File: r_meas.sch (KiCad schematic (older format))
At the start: 16 parts

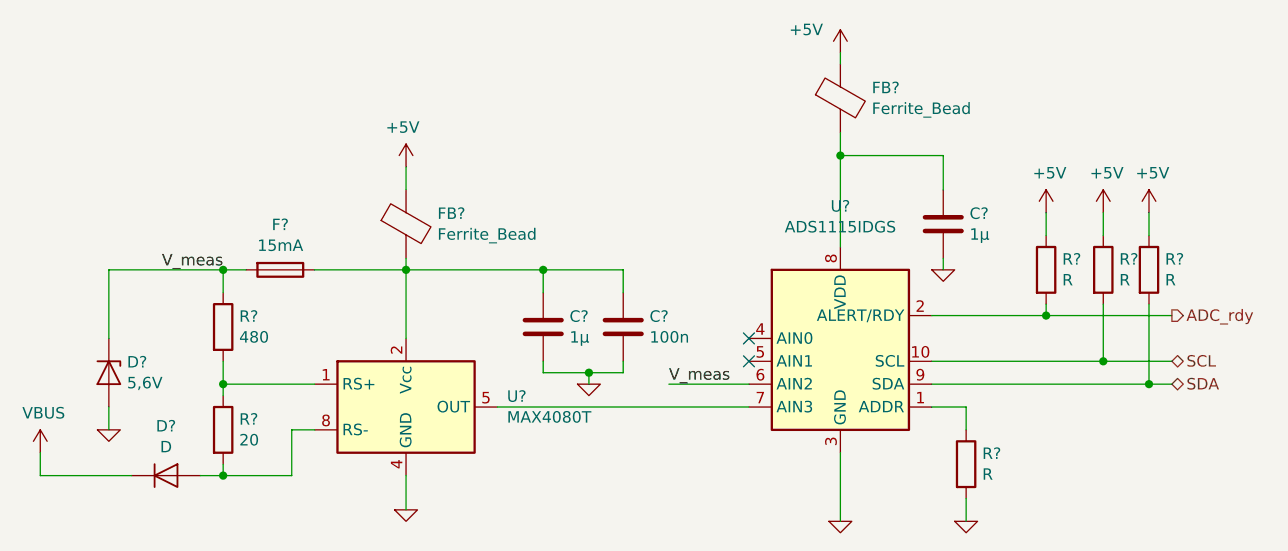
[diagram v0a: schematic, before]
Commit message: added pdf schematic
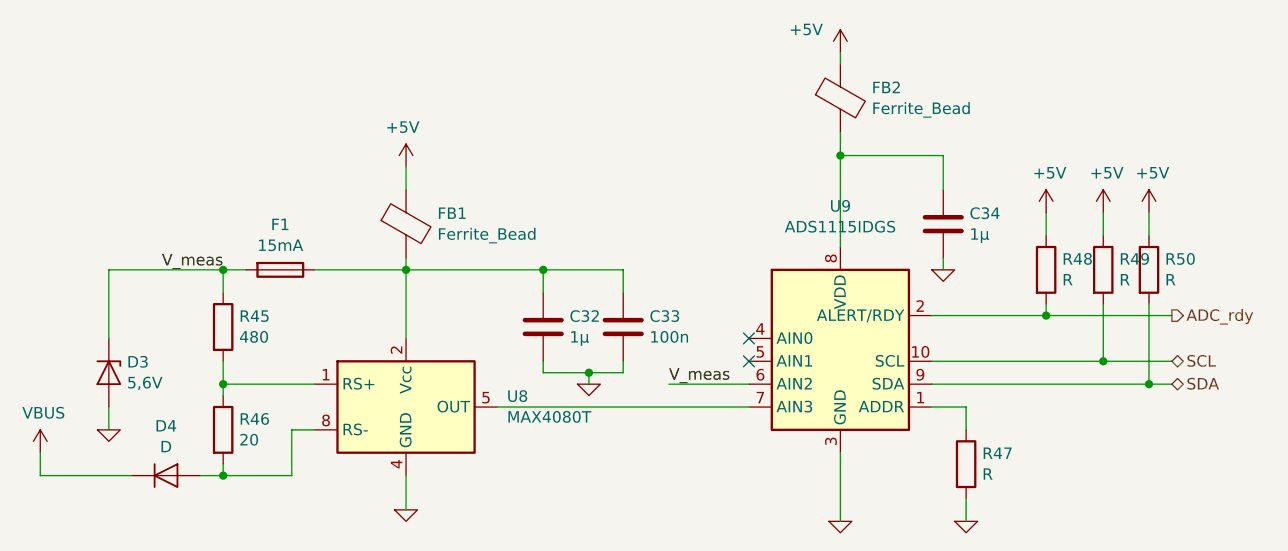
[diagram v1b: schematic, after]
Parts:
- gave numbers to parts that had none: 16
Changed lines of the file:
@@
 $EndDescr
 $Comp
-L Amplifier_Current:MAX4080T U?
+L Amplifier_Current:MAX4080T U8
 U 1 1 5D5C9028
 P 4150 3800
-F 0 "U?" H 4591 3846 50  0000 L CNN
+F 0 "U8" H 4591 3846 50  0000 L CNN
 F 1 "MAX4080T" H 4591 3755 50  0000 L CNN
 F 2 "" H 4800 3100 50  0001 C CNN
@@
 $EndComp
 $Comp
-L Analog_ADC:ADS1115IDGS U?
+L Analog_ADC:ADS1115IDGS U9
 U 1 1 5D5C90C4
 P 6050 3600
-F 0 "U?" H 6050 4278 50  0000 C CNN
+F 0 "U9" H 6050 4278 50  0000 C CNN
 F 1 "ADS1115IDGS" H 6050 4187 50  0000 C CNN
 F 2 "Package_SO:TSSOP-10_3x3mm_P0.5mm" H 6050 3100 50  0001 C CNN
@@
 $EndComp
 $Comp
-L Device:R R?
+L Device:R R49
 U 1 1 5D5C910D
 P 7200 3200
-F 0 "R?" H 7270 3246 50  0000 L CNN
+F 0 "R49" H 7270 3246 50  0000 L CNN
 F 1 "R" H 7270 3155 50  0000 L CNN
 F 2 "" V 7130 3200 50  0001 C CNN
@@
 $EndComp
 $Comp
-L Device:R R?
+L Device:R R50
 U 1 1 5D5C9157
 P 7400 3200
-F 0 "R?" H 7470 3246 50  0000 L CNN
+F 0 "R50" H 7470 3246 50  0000 L CNN
 F 1 "R" H 7470 3155 50  0000 L CNN
 F 2 "" V 7330 3200 50  0001 C CNN
@@
 SDA
 $Comp
-L power:+5V #PWR?
+L power:+5V #PWR067
 U 1 1 5D5C9230
 P 7200 2950
-F 0 "#PWR?" H 7200 2800 50  0001 C CNN
+F 0 "#PWR067" H 7200 2800 50  0001 C CNN
 F 1 "+5V" H 7215 3123 50  0000 C CNN
 F 2 "" H 7200 2950 50  0001 C CNN
@@
 $EndComp
 $Comp
-L power:+5V #PWR?
+L power:+5V #PWR062
 U 1 1 5D5C925D
 P 6050 2250
-F 0 "#PWR?" H 6050 2100 50  0001 C CNN
+F 0 "#PWR062" H 6050 2100 50  0001 C CNN
 F 1 "+5V" H 5900 2350 50  0000 C CNN
 F 2 "" H 6050 2250 50  0001 C CNN
@@
 $EndComp
 $Comp
-L power:+5V #PWR?
+L power:+5V #PWR059
 U 1 1 5D5C9278
 P 4150 2750
-F 0 "#PWR?" H 4150 2600 50  0001 C CNN
+F 0 "#PWR059" H 4150 2600 50  0001 C CNN
 F 1 "+5V" H 4165 2923 50  0000 C CNN
 F 2 "" H 4150 2750 50  0001 C CNN
@@
 $EndComp
 $Comp
-L power:+5V #PWR?
+L power:+5V #PWR068
 U 1 1 5D5C928B
 P 7400 2950
-F 0 "#PWR?" H 7400 2800 50  0001 C CNN
+F 0 "#PWR068" H 7400 2800 50  0001 C CNN
 F 1 "+5V" H 7415 3123 50  0000 C CNN
 F 2 "" H 7400 2950 50  0001 C CNN
@@
 $EndComp
 $Comp
-L Device:C C?
+L Device:C C34
 U 1 1 5D5C92DB
 P 6500 3000
-F 0 "C?" H 6615 3046 50  0000 L CNN
+F 0 "C34" H 6615 3046 50  0000 L CNN
 F 1 "1µ" H 6615 2955 50  0000 L CNN
 F 2 "" H 6538 2850 50  0001 C CNN
@@
 $EndComp
 $Comp
-L Device:Ferrite_Bead FB?
+L Device:Ferrite_Bead FB1
 U 1 1 5D5C936F
 P 4150 3000
-F 0 "FB?" H 4287 3046 50  0000 L CNN
+F 0 "FB1" H 4287 3046 50  0000 L CNN
 F 1 "Ferrite_Bead" H 4287 2955 50  0000 L CNN
 F 2 "" V 4080 3000 50  0001 C CNN
@@
 	6050 2700 6050 3100
 $Comp
-L daisy:GND #PWR?
+L daisy:GND #PWR064
 U 1 1 5D5C9638
 P 6500 3200
-F 0 "#PWR?" H 6500 3200 30  0001 C CNN
+F 0 "#PWR064" H 6500 3200 30  0001 C CNN
 F 1 "GND" H 6500 3130 30  0001 C CNN
 F 2 "" H 6500 3200 60  0000 C CNN
@@
 	7400 2950 7400 3050
 $Comp
-L Device:R R?
+L Device:R R47
 U 1 1 5D5C9A6F
 P 6600 4050
-F 0 "R?" H 6670 4096 50  0000 L CNN
+F 0 "R47" H 6670 4096 50  0000 L CNN
 F 1 "R" H 6670 4005 50  0000 L CNN
 F 2 "" V 6530 4050 50  0001 C CNN
@@
 $EndComp
 $Comp
-L daisy:GND #PWR?
+L daisy:GND #PWR065
 U 1 1 5D5C9AED
 P 6600 4300
-F 0 "#PWR?" H 6600 4300 30  0001 C CNN
+F 0 "#PWR065" H 6600 4300 30  0001 C CNN
 F 1 "GND" H 6600 4230 30  0001 C CNN
 F 2 "" H 6600 4300 60  0000 C CNN
@@
 $EndComp
 $Comp
-L daisy:GND #PWR?
+L daisy:GND #PWR063
 U 1 1 5D5C9B06
 P 6050 4300
-F 0 "#PWR?" H 6050 4300 30  0001 C CNN
+F 0 "#PWR063" H 6050 4300 30  0001 C CNN
 F 1 "GND" H 6050 4230 30  0001 C CNN
 F 2 "" H 6050 4300 60  0000 C CNN
@@
 	5650 3800 4550 3800
 $Comp
-L daisy:GND #PWR?
+L daisy:GND #PWR060
 U 1 1 5D5CA317
 P 4150 4250
-F 0 "#PWR?" H 4150 4250 30  0001 C CNN
+F 0 "#PWR060" H 4150 4250 30  0001 C CNN
 F 1 "GND" H 4150 4180 30  0001 C CNN
 F 2 "" H 4150 4250 60  0000 C CNN
@@
 	4150 4250 4150 4100
 $Comp
-L Device:C C?
+L Device:C C32
 U 1 1 5D5CA738
 P 4750 3450
-F 0 "C?" H 4865 3496 50  0000 L CNN
+F 0 "C32" H 4865 3496 50  0000 L CNN
 F 1 "1µ" H 4865 3405 50  0000 L CNN
 F 2 "" H 4788 3300 50  0001 C CNN
@@
 	4150 2850 4150 2750
 $Comp
-L Device:C C?
+L Device:C C33
 U 1 1 5D5CAD2B
 P 5100 3450
-F 0 "C?" H 5215 3496 50  0000 L CNN
+F 0 "C33" H 5215 3496 50  0000 L CNN
 F 1 "100n" H 5215 3405 50  0000 L CNN
 F 2 "" H 5138 3300 50  0001 C CNN
@@
 	4950 3650 5100 3650
 $Comp
-L daisy:GND #PWR?
+L daisy:GND #PWR061
 U 1 1 5D5CBDC2
 P 4950 3700
-F 0 "#PWR?" H 4950 3700 30  0001 C CNN
+F 0 "#PWR061" H 4950 3700 30  0001 C CNN
 F 1 "GND" H 4950 3630 30  0001 C CNN
 F 2 "" H 4950 3700 60  0000 C CNN
@@
 $EndComp
 $Comp
-L Device:Fuse F?
+L Device:Fuse F1
 U 1 1 5D5CC9A1
 P 3600 3200
-F 0 "F?" V 3403 3200 50  0000 C CNN
+F 0 "F1" V 3403 3200 50  0000 C CNN
 F 1 "15mA" V 3494 3200 50  0000 C CNN
 F 2 "" V 3530 3200 50  0001 C CNN
@@
 	3750 3200 4150 3200
 $Comp
-L Device:D_Zener D?
+L Device:D_Zener D3
 U 1 1 5D5CD013
 P 2850 3650
-F 0 "D?" V 2804 3729 50  0000 L CNN
+F 0 "D3" V 2804 3729 50  0000 L CNN
 F 1 "5,6V" V 2895 3729 50  0000 L CNN
 F 2 "" H 2850 3650 50  0001 C CNN
@@
 $EndComp
 $Comp
-L Device:R R?
+L Device:R R45
 U 1 1 5D5CD0A1
 P 3350 3450
-F 0 "R?" H 3420 3496 50  0000 L CNN
+F 0 "R45" H 3420 3496 50  0000 L CNN
 F 1 "480" H 3420 3405 50  0000 L CNN
 F 2 "" V 3280 3450 50  0001 C CNN
@@
 $EndComp
 $Comp
-L Device:R R?
+L Device:R R46
 U 1 1 5D5CD0E5
 P 3350 3900
-F 0 "R?" H 3420 3946 50  0000 L CNN
+F 0 "R46" H 3420 3946 50  0000 L CNN
 F 1 "20" H 3420 3855 50  0000 L CNN
 F 2 "" V 3280 3900 50  0001 C CNN
@@
 $EndComp
 $Comp
-L daisy:GND #PWR?
+L daisy:GND #PWR058
 U 1 1 5D5CD174
 P 2850 3900
-F 0 "#PWR?" H 2850 3900 30  0001 C CNN
+F 0 "#PWR058" H 2850 3900 30  0001 C CNN
 F 1 "GND" H 2850 3830 30  0001 C CNN
 F 2 "" H 2850 3900 60  0000 C CNN
@@
 	5300 3700 5650 3700
 $Comp
-L Device:Ferrite_Bead FB?
+L Device:Ferrite_Bead FB2
 U 1 1 5D5D2DEC
 P 6050 2450
-F 0 "FB?" H 6187 2496 50  0000 L CNN
+F 0 "FB2" H 6187 2496 50  0000 L CNN
 F 1 "Ferrite_Bead" H 6187 2405 50  0000 L CNN
 F 2 "" V 5980 2450 50  0001 C CNN
@@
 $EndComp
 $Comp
-L Device:D D?
+L Device:D D4
 U 1 1 5D5D348E
 P 3100 4100
-F 0 "D?" H 3100 4316 50  0000 C CNN
+F 0 "D4" H 3100 4316 50  0000 C CNN
 F 1 "D" H 3100 4225 50  0000 C CNN
 F 2 "" H 3100 4100 50  0001 C CNN
@@
 Connection ~ 3350 4100
 $Comp
-L power:VBUS #PWR?
+L power:VBUS #PWR057
 U 1 1 5D5D4099
 P 2550 4000
-F 0 "#PWR?" H 2550 3850 50  0001 C CNN
+F 0 "#PWR057" H 2550 3850 50  0001 C CNN
 F 1 "VBUS" H 2565 4173 50  0000 C CNN
 F 2 "" H 2550 4000 50  0001 C CNN
@@
 	2550 4100 2550 4000
 $Comp
-L Device:R R?
+L Device:R R48
 U 1 1 5D5D66BA
 P 6950 3200
-F 0 "R?" H 7020 3246 50  0000 L CNN
+F 0 "R48" H 7020 3246 50  0000 L CNN
 F 1 "R" H 7020 3155 50  0000 L CNN
 F 2 "" V 6880 3200 50  0001 C CNN
@@
 	6950 3400 6950 3350
 $Comp
-L power:+5V #PWR?
+L power:+5V #PWR066
 U 1 1 5D5DCDE2
 P 6950 2950
-F 0 "#PWR?" H 6950 2800 50  0001 C CNN
+F 0 "#PWR066" H 6950 2800 50  0001 C CNN
 F 1 "+5V" H 6965 3123 50  0000 C CNN
 F 2 "" H 6950 2950 50  0001 C CNN

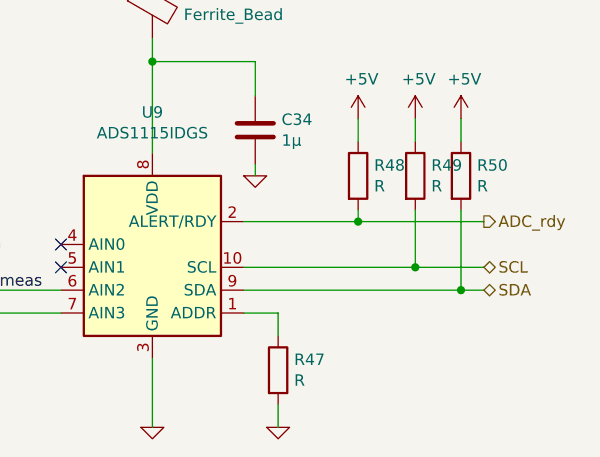
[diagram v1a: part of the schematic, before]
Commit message: started assigning footprints
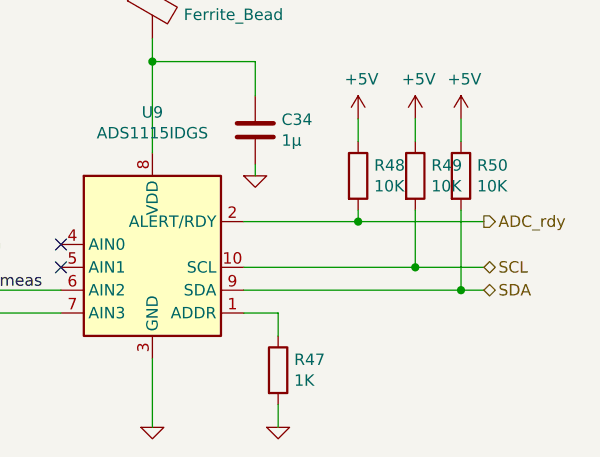
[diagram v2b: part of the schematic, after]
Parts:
- C32, C34: footprint (none) -> Capacitor_SMD:C_1206_3216Metric
- C33: footprint (none) -> Capacitor_SMD:C_0603_1608Metric
- D3, D4: footprint (none) -> Diode_SMD:D_1206_3216Metric
- F1: footprint (none) -> Fuse:Fuse_1206_3216Metric
- FB1, FB2: footprint (none) -> Inductor_SMD:L_1206_3216Metric
- R45, R46: footprint (none) -> Resistor_SMD:R_0603_1608Metric
- R47: value R -> 1K; footprint (none) -> Resistor_SMD:R_0603_1608Metric
- R48, R49, R50: value R -> 10K; footprint (none) -> Resistor_SMD:R_0603_1608Metric
- U8: footprint (none) -> Package_SO:SOIC-8_3.9x4.9mm_P1.27mm
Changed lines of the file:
@@
 F 0 "U8" H 4591 3846 50  0000 L CNN
 F 1 "MAX4080T" H 4591 3755 50  0000 L CNN
-F 2 "" H 4800 3100 50  0001 C CNN
+F 2 "Package_SO:SOIC-8_3.9x4.9mm_P1.27mm" H 4800 3100 50  0001 C CNN
 F 3 "http://datasheets.maximintegrated.com/en/ds/MAX4080-MAX4081.pdf" H 4150 4200 50  0001 C CNN
 	1    4150 3800
@@
 P 7200 3200
 F 0 "R49" H 7270 3246 50  0000 L CNN
-F 1 "R" H 7270 3155 50  0000 L CNN
-F 2 "" V 7130 3200 50  0001 C CNN
+F 1 "10K" H 7270 3155 50  0000 L CNN
+F 2 "Resistor_SMD:R_0603_1608Metric" V 7130 3200 50  0001 C CNN
 F 3 "~" H 7200 3200 50  0001 C CNN
 	1    7200 3200
@@
 P 7400 3200
 F 0 "R50" H 7470 3246 50  0000 L CNN
-F 1 "R" H 7470 3155 50  0000 L CNN
-F 2 "" V 7330 3200 50  0001 C CNN
+F 1 "10K" H 7470 3155 50  0000 L CNN
+F 2 "Resistor_SMD:R_0603_1608Metric" V 7330 3200 50  0001 C CNN
 F 3 "~" H 7400 3200 50  0001 C CNN
 	1    7400 3200
@@
 F 0 "C34" H 6615 3046 50  0000 L CNN
 F 1 "1µ" H 6615 2955 50  0000 L CNN
-F 2 "" H 6538 2850 50  0001 C CNN
+F 2 "Capacitor_SMD:C_1206_3216Metric" H 6538 2850 50  0001 C CNN
 F 3 "~" H 6500 3000 50  0001 C CNN
 	1    6500 3000
@@
 F 0 "FB1" H 4287 3046 50  0000 L CNN
 F 1 "Ferrite_Bead" H 4287 2955 50  0000 L CNN
-F 2 "" V 4080 3000 50  0001 C CNN
+F 2 "Inductor_SMD:L_1206_3216Metric" V 4080 3000 50  0001 C CNN
 F 3 "~" H 4150 3000 50  0001 C CNN
 	1    4150 3000
@@
 P 6600 4050
 F 0 "R47" H 6670 4096 50  0000 L CNN
-F 1 "R" H 6670 4005 50  0000 L CNN
-F 2 "" V 6530 4050 50  0001 C CNN
+F 1 "1K" H 6670 4005 50  0000 L CNN
+F 2 "Resistor_SMD:R_0603_1608Metric" V 6530 4050 50  0001 C CNN
 F 3 "~" H 6600 4050 50  0001 C CNN
 	1    6600 4050
@@
 F 0 "C32" H 4865 3496 50  0000 L CNN
 F 1 "1µ" H 4865 3405 50  0000 L CNN
-F 2 "" H 4788 3300 50  0001 C CNN
+F 2 "Capacitor_SMD:C_1206_3216Metric" H 4788 3300 50  0001 C CNN
 F 3 "~" H 4750 3450 50  0001 C CNN
 	1    4750 3450
@@
 F 0 "C33" H 5215 3496 50  0000 L CNN
 F 1 "100n" H 5215 3405 50  0000 L CNN
-F 2 "" H 5138 3300 50  0001 C CNN
+F 2 "Capacitor_SMD:C_0603_1608Metric" H 5138 3300 50  0001 C CNN
 F 3 "~" H 5100 3450 50  0001 C CNN
 	1    5100 3450
@@
 F 0 "F1" V 3403 3200 50  0000 C CNN
 F 1 "15mA" V 3494 3200 50  0000 C CNN
-F 2 "" V 3530 3200 50  0001 C CNN
+F 2 "Fuse:Fuse_1206_3216Metric" V 3530 3200 50  0001 C CNN
 F 3 "~" H 3600 3200 50  0001 C CNN
 	1    3600 3200
@@
 F 0 "D3" V 2804 3729 50  0000 L CNN
 F 1 "5,6V" V 2895 3729 50  0000 L CNN
-F 2 "" H 2850 3650 50  0001 C CNN
+F 2 "Diode_SMD:D_1206_3216Metric" H 2850 3650 50  0001 C CNN
 F 3 "~" H 2850 3650 50  0001 C CNN
 	1    2850 3650
@@
 F 0 "R45" H 3420 3496 50  0000 L CNN
 F 1 "480" H 3420 3405 50  0000 L CNN
-F 2 "" V 3280 3450 50  0001 C CNN
+F 2 "Resistor_SMD:R_0603_1608Metric" V 3280 3450 50  0001 C CNN
 F 3 "~" H 3350 3450 50  0001 C CNN
 	1    3350 3450
@@
 F 0 "R46" H 3420 3946 50  0000 L CNN
 F 1 "20" H 3420 3855 50  0000 L CNN
-F 2 "" V 3280 3900 50  0001 C CNN
+F 2 "Resistor_SMD:R_0603_1608Metric" V 3280 3900 50  0001 C CNN
 F 3 "~" H 3350 3900 50  0001 C CNN
 	1    3350 3900
@@
 F 0 "FB2" H 6187 2496 50  0000 L CNN
 F 1 "Ferrite_Bead" H 6187 2405 50  0000 L CNN
-F 2 "" V 5980 2450 50  0001 C CNN
+F 2 "Inductor_SMD:L_1206_3216Metric" V 5980 2450 50  0001 C CNN
 F 3 "~" H 6050 2450 50  0001 C CNN
 	1    6050 2450
@@
 F 0 "D4" H 3100 4316 50  0000 C CNN
 F 1 "D" H 3100 4225 50  0000 C CNN
-F 2 "" H 3100 4100 50  0001 C CNN
+F 2 "Diode_SMD:D_1206_3216Metric" H 3100 4100 50  0001 C CNN
 F 3 "~" H 3100 4100 50  0001 C CNN
 	1    3100 4100
@@
 P 6950 3200
 F 0 "R48" H 7020 3246 50  0000 L CNN
-F 1 "R" H 7020 3155 50  0000 L CNN
-F 2 "" V 6880 3200 50  0001 C CNN
+F 1 "10K" H 7020 3155 50  0000 L CNN
+F 2 "Resistor_SMD:R_0603_1608Metric" V 6880 3200 50  0001 C CNN
 F 3 "~" H 6950 3200 50  0001 C CNN
 	1    6950 3200
